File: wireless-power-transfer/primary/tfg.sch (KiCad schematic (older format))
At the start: 31 parts, among them J1 CONN_01X06, J2 Screw_Terminal_1x02, J3 BARREL_JACK, Q1 IRLB8721PBF, Q2 IRLB8721PBF, Q3 IRLB8721PBF, Q4 IRLB8721PBF, U1 PIC18F45K20-I/PT, U2 IR2110, U3 IR2110, U4 R-78E15, U5 R-78E3.3, U6 XBEE_Wi-Fi

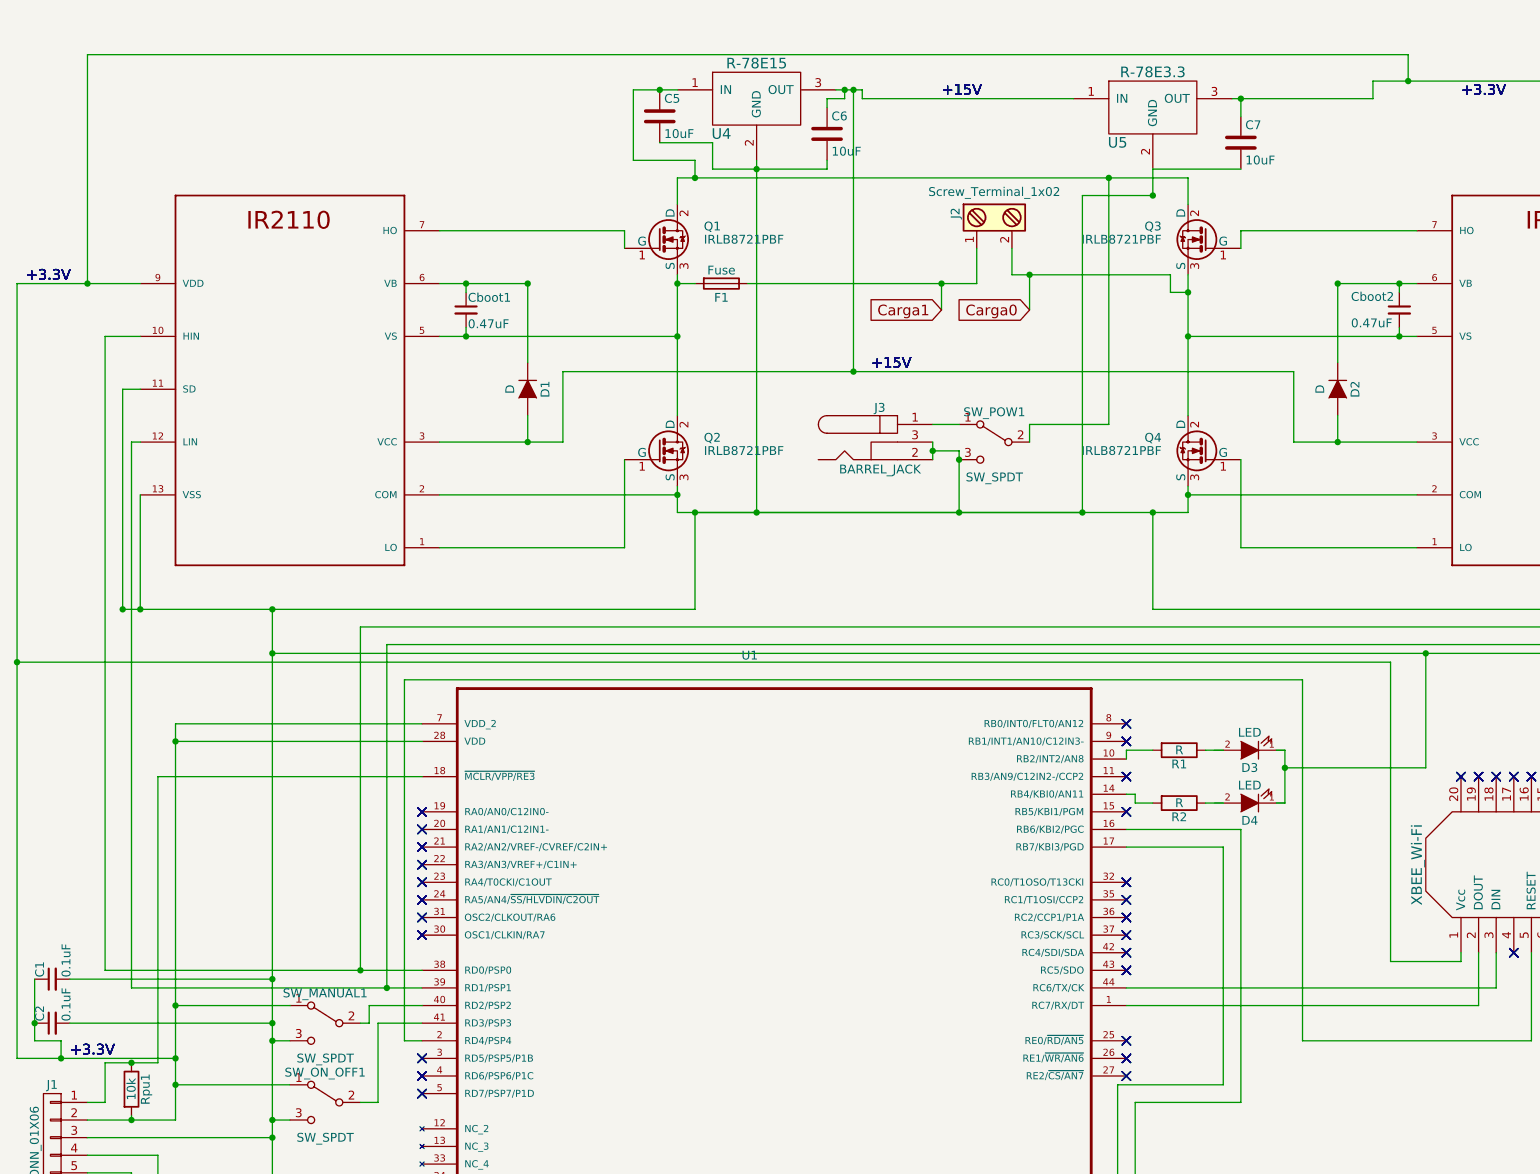
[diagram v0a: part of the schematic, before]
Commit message: Arranged component-library
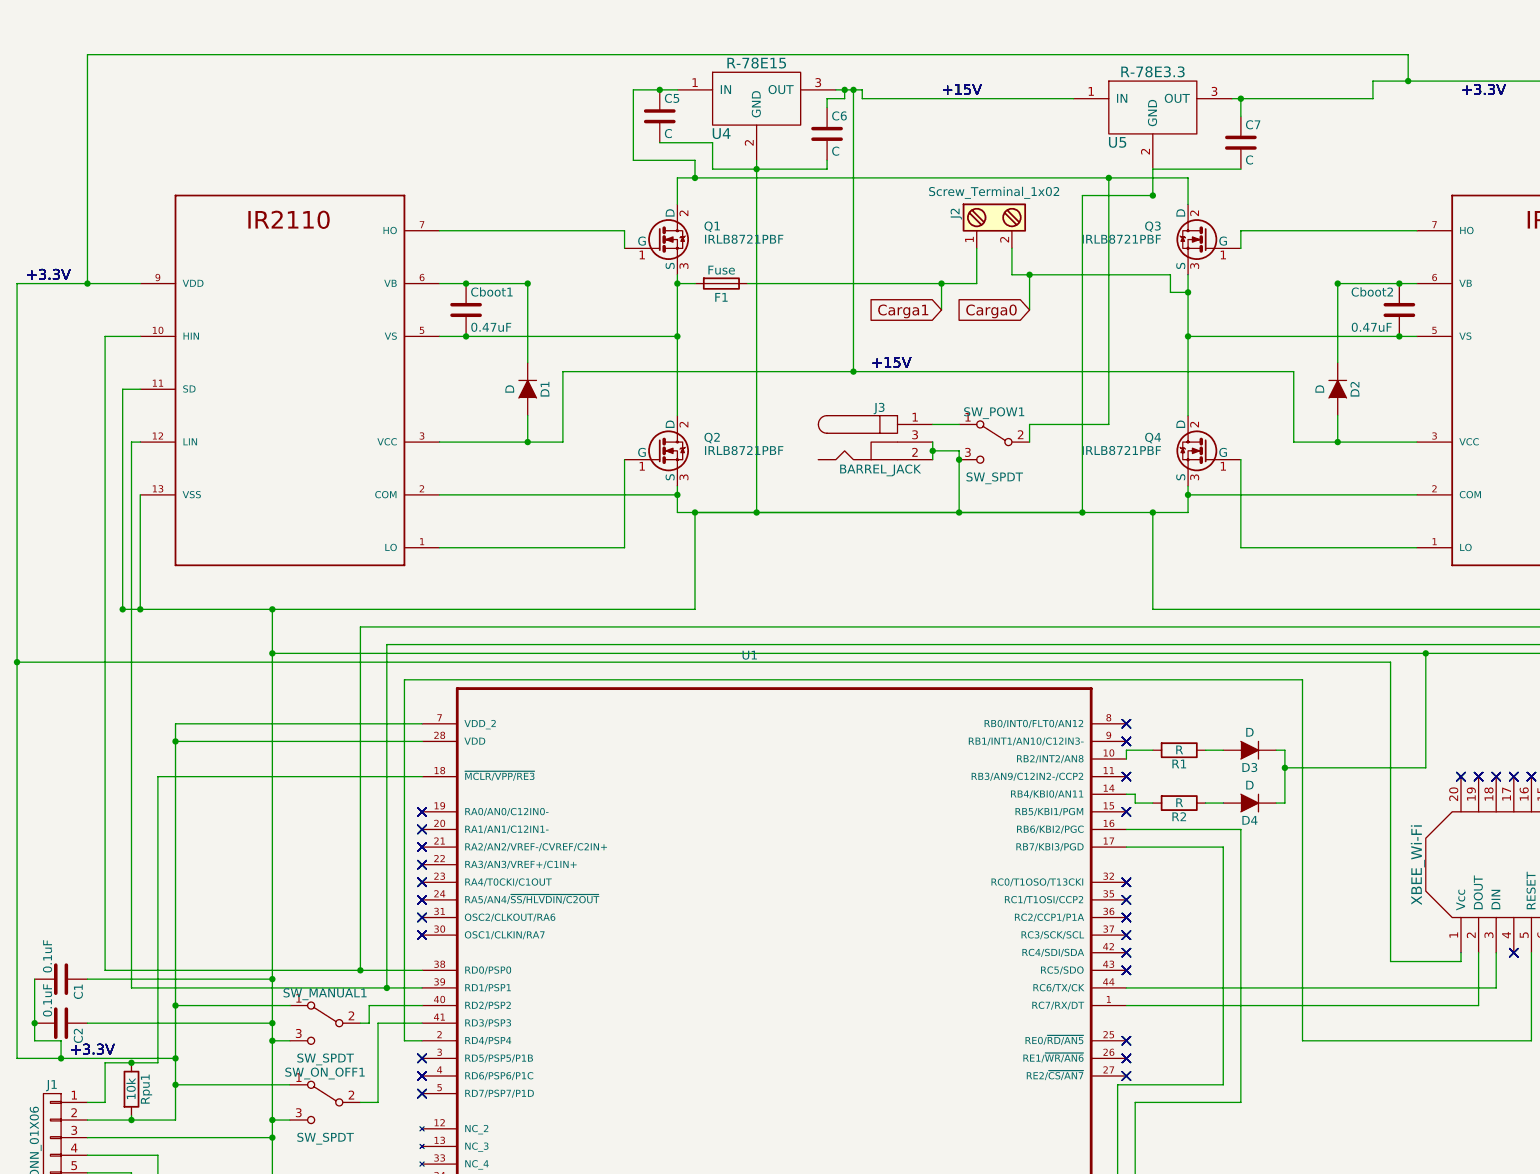
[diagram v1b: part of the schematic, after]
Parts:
- removed C1, C2: 0.1uF, Capacitors_SMD:C_1206_HandSoldering, symbol C_Small
- removed Cboot1, Cboot2: 0.47uF, Capacitors_SMD:C_1206_HandSoldering, symbol C_Small
- removed D3, D4: LED, LEDs:LED_D3.0mm, symbol LED-RESCUE-tfg
- added C1, C2: 0.1uF, symbol C
- added Cboot1, Cboot2: 0.47uF, symbol C
- added D3, D4: D, symbol D
- C5, C6, C7: value 10uF -> C; footprint Capacitors_SMD:C_1206_HandSoldering -> (none)
- D1, D2: footprint Diodes_THT:D_DO-35_SOD27_P5.08mm_Vertical_AnodeUp -> (none)
- F1: footprint Fuse_Holders_and_Fuses:Fuseholder5x20_horiz_SemiClosed_Casing10x25mm -> (none)
- J1: footprint Pin_Headers:Pin_Header_Angled_1x06_Pitch2.54mm -> (none)
- J2: footprint Connectors_Terminal_Blocks:TerminalBlock_Pheonix_MKDS1.5-2pol -> (none)
- J3: footprint Connectors:BARREL_JACK -> (none)
- Q1, Q2, Q3, Q4: footprint componentesGIT:TO-247AC -> TO_SOT_Packages_THT:TO-220_Vertical
- R1, R2, Rpu1: footprint Resistors_SMD:R_1206_HandSoldering -> (none)
- SW_MANUAL1, SW_ON_OFF1, SW_POW1: footprint componentes:SPDT_Toggle_Switch -> (none)
- U1: footprint componentesGIT:PIC18F45K20 -> QFP80P1200X1200X120-44N
- U2, U3: footprint Housings_DIP:DIP-14_W7.62mm -> DIL14-1; Availability Unavailable -> (none); Price 2.97 USD -> (none)
- U4, U5: footprint componentes:r-78Exx -> (none)
- U6: footprint componentes:XBee_Wi-Fi -> (none)
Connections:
- net +3.3V: now also C1.2, C2.2
- net Carga0: now also Cboot2.2
- net at C5.2, C6.2, C7.2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: now also C1.1, C2.1, D3.1 (K), D4.1 (K)
- net at F1.2, Q1.3 (S), Q2.2 (D)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: now also Cboot1.2
- net at D1.1 (K), U2.6 (VB): now also Cboot1.1
- net at D2.1 (K), U3.6 (VB): now also Cboot2.1
- net at R1.1: now also D3.2 (A)
- net at R2.1: now also D4.2 (A)

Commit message: Schematics and footprint libraries ready
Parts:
- removed D3, D4: D, symbol D
- added D3, D4: LED_ALT, symbol LED_ALT
- Cboot1, Cboot2: value 0.47uF -> C
- J1: footprint (none) -> footprint:Pin_Header_Angled_1x06_Pitch2.54mm
- R1, R2: value R -> 100
- SW_MANUAL1, SW_ON_OFF1: footprint (none) -> footprint:SPDT_Toggle_Switch
- U1: footprint QFP80P1200X1200X120-44N -> footprint:PIC18F45K20
- U6: footprint (none) -> footprint:XBee_Wi-Fi
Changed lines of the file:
@@
 	9400 2700 9400 2500
 Connection ~ 9400 2500
+Wire Wire Line
+	5100 6500 4050 6500
+Wire Wire Line
+	4050 6750 5100 6750
 $Comp
 L PIC18F45K20-I/PT U1
-U 1 1 5A9EC8B8
+U 1 1 5AA66D8B
 P 7950 6350
 F 0 "U1" H 7764 8009 50  0000 L BNN
 F 1 "PIC18F45K20-I/PT" H 7629 4416 50  0000 L BNN
-F 2 "QFP80P1200X1200X120-44N" H 9760 4270 50  0001 L BNN
+F 2 "footprint:PIC18F45K20" H 9760 4270 50  0001 L BNN
 F 3 "2.16 USD" H 9720 7915 50  0001 L BNN
 F 4 "TQFP-44 10x10x1mm Tray%2C 32KB%2C Flash%2C 1536bytes-RAM%2C 36I/O%2C 8-Bit nanoWatt" H 6135 4090 50  0001 L BNN "Description"
@@
 $EndComp
 $Comp
+L R R1
+U 1 1 5AA673A2
+P 10250 5200
+F 0 "R1" V 10330 5200 50  0000 C CNN
+F 1 "100" V 10250 5200 50  0000 C CNN
+F 2 "" V 10180 5200 50  0001 C CNN
+F 3 "" H 10250 5200 50  0001 C CNN
+	1    10250 5200
+	0    1    1    0
+$EndComp
+$Comp
+L R R2
+U 1 1 5AA67437
+P 10250 5500
+F 0 "R2" V 10330 5500 50  0000 C CNN
+F 1 "100" V 10250 5500 50  0000 C CNN
+F 2 "" V 10180 5500 50  0001 C CNN
+F 3 "" H 10250 5500 50  0001 C CNN
+	1    10250 5500
+	0    1    1    0
+$EndComp
+$Comp
+L LED_ALT D3
+U 1 1 5AA6772E
+P 10650 5200
+F 0 "D3" H 10650 5300 50  0000 C CNN
+F 1 "LED_ALT" H 10650 5100 50  0000 C CNN
+F 2 "" H 10650 5200 50  0001 C CNN
+F 3 "" H 10650 5200 50  0001 C CNN
+	1    10650 5200
+	-1   0    0    1
+$EndComp
+$Comp
+L LED_ALT D4
+U 1 1 5AA677BF
+P 10650 5500
+F 0 "D4" H 10650 5600 50  0000 C CNN
+F 1 "LED_ALT" H 10650 5400 50  0000 C CNN
+F 2 "" H 10650 5500 50  0001 C CNN
+F 3 "" H 10650 5500 50  0001 C CNN
+	1    10650 5500
+	-1   0    0    1
+$EndComp
+$Comp
+L XBEE_Wi-Fi U6
+U 1 1 5AA67B00
+P 12100 5850
+F 0 "U6" H 12900 5850 60  0000 C CNN
+F 1 "XBEE_Wi-Fi" V 11600 5850 60  0000 C CNN
+F 2 "footprint:XBee_Wi-Fi" H 12100 5850 60  0001 C CNN
+F 3 "" H 12100 5850 60  0001 C CNN
+	1    12100 5850
+	1    0    0    -1
+$EndComp
+$Comp
 L SW_SPDT SW_MANUAL1
-U 1 1 5A9ECE65
+U 1 1 5AA68056
 P 5400 6750
 F 0 "SW_MANUAL1" H 5400 6920 50  0000 C CNN
 F 1 "SW_SPDT" H 5400 6550 50  0000 C CNN
-F 2 "" H 5400 6750 50  0001 C CNN
+F 2 "footprint:SPDT_Toggle_Switch" H 5400 6750 50  0001 C CNN
 F 3 "" H 5400 6750 50  0001 C CNN
 	1    5400 6750
@@
 $Comp
 L SW_SPDT SW_ON_OFF1
-U 1 1 5A9ECFFF
+U 1 1 5AA68133
 P 5400 7200
 F 0 "SW_ON_OFF1" H 5400 7370 50  0000 C CNN
 F 1 "SW_SPDT" H 5400 7000 50  0000 C CNN
-F 2 "" H 5400 7200 50  0001 C CNN
+F 2 "footprint:SPDT_Toggle_Switch" H 5400 7200 50  0001 C CNN
 F 3 "" H 5400 7200 50  0001 C CNN
 	1    5400 7200
@@
 $Comp
 L R Rpu1
-U 1 1 5A9ED086
+U 1 1 5AA681F1
 P 4300 7125
 F 0 "Rpu1" V 4380 7125 50  0000 C CNN
@@
 $Comp
 L CONN_01X06 J1
-U 1 1 5A9EE4EB
+U 1 1 5AA68E1B
 P 3850 7450
 F 0 "J1" H 3850 7800 50  0000 C CNN
 F 1 "CONN_01X06" V 3950 7450 50  0000 C CNN
-F 2 "" H 3850 7450 50  0001 C CNN
+F 2 "footprint:Pin_Header_Angled_1x06_Pitch2.54mm" H 3850 7450 50  0001 C CNN
 F 3 "" H 3850 7450 50  0001 C CNN
 	1    3850 7450
@@
 $Comp
 L C C1
-U 1 1 5A9EE744
+U 1 1 5AA6923F
 P 3900 6500
 F 0 "C1" H 3925 6600 50  0000 L CNN
-F 1 "0.1uF" H 3675 6425 50  0000 L CNN
+F 1 "0.1uF" H 3925 6400 50  0000 L CNN
 F 2 "" H 3938 6350 50  0001 C CNN
 F 3 "" H 3900 6500 50  0001 C CNN
 	1    3900 6500
-	0    1    1    0
+	0    -1   -1   0
 $EndComp
 $Comp
 L C C2
-U 1 1 5A9EE7CD
+U 1 1 5AA692BC
 P 3900 6750
 F 0 "C2" H 3925 6850 50  0000 L CNN
-F 1 "0.1uF" H 3675 6675 50  0000 L CNN
+F 1 "0.1uF" H 3925 6650 50  0000 L CNN
 F 2 "" H 3938 6600 50  0001 C CNN
 F 3 "" H 3900 6750 50  0001 C CNN
 	1    3900 6750
-	0    1    1    0
-$EndComp
-Wire Wire Line
-	5100 6500 4050 6500
-Wire Wire Line
-	4050 6750 5100 6750
-$Comp
-L R R1
-U 1 1 5A9EF3C8
-P 10250 5200
-F 0 "R1" V 10330 5200 50  0000 C CNN
-F 1 "R" V 10250 5200 50  0000 C CNN
-F 2 "" V 10180 5200 50  0001 C CNN
-F 3 "" H 10250 5200 50  0001 C CNN
-	1    10250 5200
-	0    1    1    0
-$EndComp
-$Comp
-L R R2
-U 1 1 5A9EF549
-P 10250 5500
-F 0 "R2" V 10330 5500 50  0000 C CNN
-F 1 "R" V 10250 5500 50  0000 C CNN
-F 2 "" V 10180 5500 50  0001 C CNN
-F 3 "" H 10250 5500 50  0001 C CNN
-	1    10250 5500
-	0    1    1    0
-$EndComp
-$Comp
-L D D3
-U 1 1 5A9EF6A5
-P 10650 5200
-F 0 "D3" H 10650 5300 50  0000 C CNN
-F 1 "D" H 10650 5100 50  0000 C CNN
-F 2 "" H 10650 5200 50  0001 C CNN
-F 3 "" H 10650 5200 50  0001 C CNN
-	1    10650 5200
-	-1   0    0    1
-$EndComp
-$Comp
-L D D4
-U 1 1 5A9EF742
-P 10650 5500
-F 0 "D4" H 10650 5600 50  0000 C CNN
-F 1 "D" H 10650 5400 50  0000 C CNN
-F 2 "" H 10650 5500 50  0001 C CNN
-F 3 "" H 10650 5500 50  0001 C CNN
-	1    10650 5500
-	-1   0    0    1
-$EndComp
-$Comp
-L XBEE_Wi-Fi U6
-U 1 1 5A9EFB50
-P 12100 5850
-F 0 "U6" H 12900 5850 60  0000 C CNN
-F 1 "XBEE_Wi-Fi" V 11600 5850 60  0000 C CNN
-F 2 "" H 12100 5850 60  0001 C CNN
-F 3 "" H 12100 5850 60  0001 C CNN
-	1    12100 5850
-	1    0    0    -1
+	0    -1   -1   0
 $EndComp
 $Comp
 L IR2110 U2
-U 1 1 5A9F073F
+U 1 1 5AA6A0D8
 P 5250 3050
 F 0 "U2" H 5185 4110 50  0001 L BNN
@@
 $Comp
 L IR2110 U3
-U 1 1 5A9F096F
+U 1 1 5AA6A4D1
 P 12400 3050
 F 0 "U3" H 12335 4110 50  0001 L BNN
@@
 $Comp
 L C Cboot1
-U 1 1 5A9F1AAA
+U 1 1 5AA6A944
 P 6200 2700
 F 0 "Cboot1" H 6225 2800 50  0000 L CNN
-F 1 "0.47uF" H 6225 2600 50  0000 L CNN
+F 1 "C" H 6225 2600 50  0000 L CNN
 F 2 "" H 6238 2550 50  0001 C CNN
 F 3 "" H 6200 2700 50  0001 C CNN
@@
 $EndComp
 $Comp
+L C Cboot2
+U 1 1 5AA6A9BD
+P 11500 2700
+F 0 "Cboot2" H 11525 2800 50  0000 L CNN
+F 1 "C" H 11525 2600 50  0000 L CNN
+F 2 "" H 11538 2550 50  0001 C CNN
+F 3 "" H 11500 2700 50  0001 C CNN
+	1    11500 2700
+	1    0    0    -1
+$EndComp
+$Comp
 L D D1
-U 1 1 5A9F1E2D
+U 1 1 5AA6BB5F
 P 6550 3150
 F 0 "D1" H 6550 3250 50  0000 C CNN
@@
 $EndComp
 $Comp
-L C Cboot2
-U 1 1 5A9F2557
-P 11500 2700
-F 0 "Cboot2" H 11225 2800 50  0000 L CNN
-F 1 "0.47uF" H 11225 2600 50  0000 L CNN
-F 2 "" H 11538 2550 50  0001 C CNN
-F 3 "" H 11500 2700 50  0001 C CNN
-	1    11500 2700
-	1    0    0    -1
-$EndComp
-$Comp
 L D D2
-U 1 1 5A9F3CFB
+U 1 1 5AA6BBE2
 P 11150 3150
 F 0 "D2" H 11150 3250 50  0000 C CNN
@@
 $Comp
 L IRLB8721PBF Q1
-U 1 1 5A9F4065
+U 1 1 5AA6C352
 P 7300 2300
 F 0 "Q1" H 7550 2375 50  0000 L CNN
@@
 $Comp
 L IRLB8721PBF Q2
-U 1 1 5A9F421C
+U 1 1 5AA6C45D
 P 7300 3500
 F 0 "Q2" H 7550 3575 50  0000 L CNN
@@
 $Comp
 L IRLB8721PBF Q3
-U 1 1 5A9F429B
+U 1 1 5AA6C4F4
 P 10400 2300
 F 0 "Q3" H 10650 2375 50  0000 L CNN
@@
 $Comp
 L IRLB8721PBF Q4
-U 1 1 5A9F433F
+U 1 1 5AA6C636
 P 10400 3500
 F 0 "Q4" H 10650 3575 50  0000 L CNN
@@
 $EndComp
 $Comp
-L SW_SPDT SW_POW1
-U 1 1 5A9F4591
-P 9200 3450
-F 0 "SW_POW1" H 9200 3620 50  0000 C CNN
-F 1 "SW_SPDT" H 9200 3250 50  0000 C CNN
-F 2 "" H 9200 3450 50  0001 C CNN
-F 3 "" H 9200 3450 50  0001 C CNN
-	1    9200 3450
-	-1   0    0    -1
-$EndComp
-$Comp
 L BARREL_JACK J3
-U 1 1 5A9F4652
+U 1 1 5AA6D707
 P 8550 3450
 F 0 "J3" H 8550 3645 50  0000 C CNN
@@
 $Comp
 L Screw_Terminal_1x02 J2
-U 1 1 5A9F4D48
+U 1 1 5AA6DA58
 P 9200 2150
 F 0 "J2" H 9200 2400 50  0000 C TNN
@@
 $EndComp
 $Comp
+L Fuse F1
+U 1 1 5AA6DCF9
+P 7650 2550
+F 0 "F1" V 7730 2550 50  0000 C CNN
+F 1 "Fuse" V 7575 2550 50  0000 C CNN
+F 2 "" V 7580 2550 50  0001 C CNN
+F 3 "" H 7650 2550 50  0001 C CNN
+	1    7650 2550
+	0    1    1    0
+$EndComp
+$Comp
+L SW_SPDT SW_POW1
+U 1 1 5AA6DFD9
+P 9200 3450
+F 0 "SW_POW1" H 9200 3620 50  0000 C CNN
+F 1 "SW_SPDT" H 9200 3250 50  0000 C CNN
+F 2 "" H 9200 3450 50  0001 C CNN
+F 3 "" H 9200 3450 50  0001 C CNN
+	1    9200 3450
+	-1   0    0    -1
+$EndComp
+$Comp
 L C C5
-U 1 1 5A9F5163
+U 1 1 5AA6E26B
 P 7300 1600
 F 0 "C5" H 7325 1700 50  0000 L CNN
@@
 $Comp
 L C C6
-U 1 1 5A9F51ED
+U 1 1 5AA6E30C
 P 8250 1700
 F 0 "C6" H 8275 1800 50  0000 L CNN
@@
 $Comp
 L C C7
-U 1 1 5A9F5289
+U 1 1 5AA6E444
 P 10600 1750
 F 0 "C7" H 10625 1850 50  0000 L CNN
@@
 $Comp
 L R-78E3.3 U4
-U 1 1 5A9F587D
+U 1 1 5AA6FB0D
 P 7850 1450
 F 0 "U4" H 7650 1200 60  0000 C CNN
@@
 $Comp
 L R-78E3.3 U5
-U 1 1 5A9F592E
+U 1 1 5AA6FB94
 P 10100 1500
 F 0 "U5" H 9900 1250 60  0000 C CNN
@@
 	1    0    0    -1
 $EndComp
-$Comp
-L Fuse F1
-U 1 1 5A9F6809
-P 7650 2550
-F 0 "F1" V 7730 2550 50  0000 C CNN
-F 1 "Fuse" V 7575 2550 50  0000 C CNN
-F 2 "" V 7580 2550 50  0001 C CNN
-F 3 "" H 7650 2550 50  0001 C CNN
-	1    7650 2550
-	0    1    1    0
-$EndComp
 $EndSCHEMATC
